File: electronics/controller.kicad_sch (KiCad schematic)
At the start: 88 parts, among them J1 Power_Supply_Connector, J10 Heated_Bed_Thermistor_Connect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, J11 Bl_Touch_Gnd_ZMin_Connector, J12 Bl_Touch_Signal_Vcc_Gnd_Conne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, J13 Motor_A_Connector, J14 Motor_B_Connector, J15 Motor_Z_Connector, J16 Motor_E_Connector, J2 X_Axis_Endstop_Connector, J3 Y_Axis_Endstop_Connector, J4 USB_C_Receptacle_USB2.0, J5 Hotend_Connector, J6 Heated_Bed_Connector, J7 Hotend_Fan_Connector, J8 Layer_Fan_Connector, J9 Hotend_Thermistor_Connector, Q1 PSMN4R1-30YLC, Q2 PSMN4R1-30YLC, Q3 PSMN4R1-30YLC, Q4 PSMN4R1-30YLC, SW1 EN_Button, SW2 Boot_Button, SW3 Pause/Resume_Button, U1 AZ1084CD-3.3TRG1, U10 MCU45P04-TP, U11 K7805MT-1000R4, U3 ESP32-S3-WROOM-1, U4 MT29F2G01ABAGDWB-IT, U5 USBLC6-2SC6, U6 TMC2209_SILENTSTEPSTICK, U7 TMC2209_SILENTSTEPSTICK, U8 TMC2209_SILENTSTEPSTICK, U9 TMC2209_SILENTSTEPSTICK

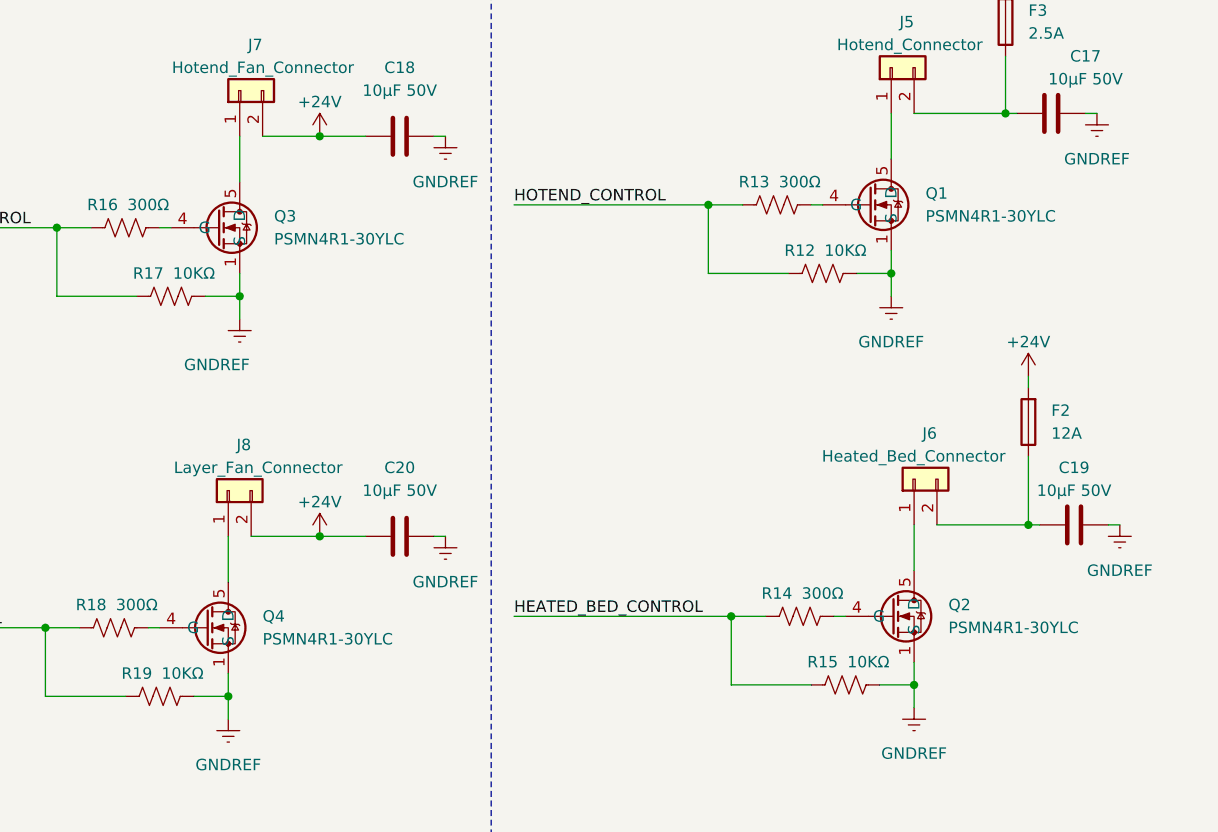
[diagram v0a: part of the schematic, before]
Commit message: ⚡️ Replace the PSMN4R1-30YLC mosfets with the appropriate ones on KiCad schematic
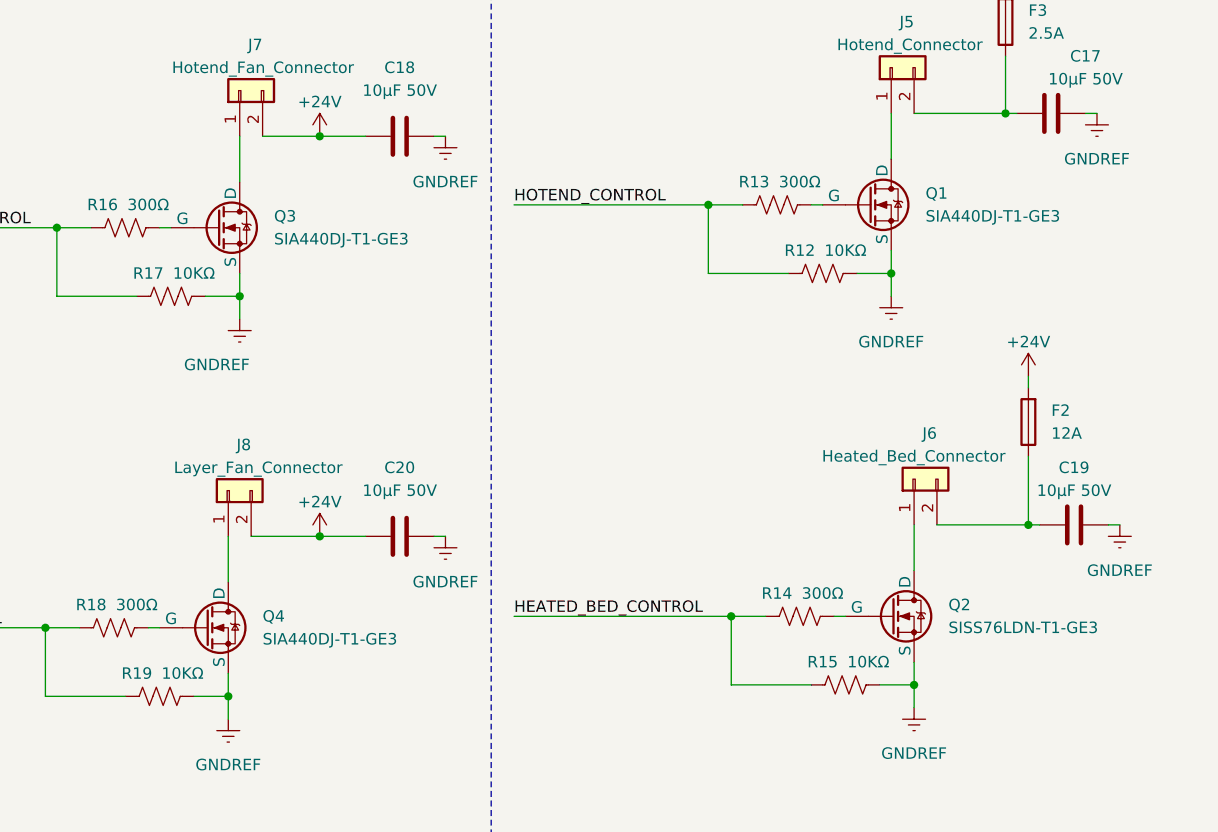
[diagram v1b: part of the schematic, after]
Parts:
- Q1, Q3, Q4: value PSMN4R1-30YLC -> SIA440DJ-T1-GE3; symbol Project:PSMN4R1-30YLC -> Project:NMOS
- Q2: value PSMN4R1-30YLC -> SISS76LDN-T1-GE3; symbol Project:PSMN4R1-30YLC -> Project:NMOS
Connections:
- net GNDREF: no longer Q1.1 (S), Q1.2 (S), Q2.1 (S), Q2.2 (S), Q3.1 (S), Q3.2 (S), Q4.1 (S), Q4.2 (S)
- net at J5.1 (Pin_1): now also Q1.1 (D); no longer Q1.5 (D)
- net at R14.2: now also Q2.2 (G); no longer Q2.4 (G)
- net at J6.1 (Pin_1): now also Q2.1 (D); no longer Q2.5 (D)
- net at R18.2: now also Q4.2 (G); no longer Q4.4 (G)
- net at J8.1 (Pin_1): now also Q4.1 (D); no longer Q4.5 (D)
- net at J7.1 (Pin_1): now also Q3.1 (D); no longer Q3.5 (D)
- net at R13.2: now also Q1.2 (G); no longer Q1.4 (G)
- net at R16.2: now also Q3.2 (G); no longer Q3.4 (G)
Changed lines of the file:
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@@
     )
   )
-  (symbol (lib_id "Project:PSMN4R1-30YLC") (at 374.65 228.6 0) (unit 1)
+  (symbol (lib_id "Project:NMOS") (at 374.65 228.6 0) (unit 1)
     (in_bom yes) (on_board yes) (dnp no) (fields_autoplaced)
     (property "Reference" "Q2" (at 381 227.33 0)
       (effects (font (size 1.27 1.27)) (justify left))
     )
-    (property "Value" "PSMN4R1-30YLC" (at 381 229.87 0)
+    (property "Value" "SISS76LDN-T1-GE3" (at 381 229.87 0)
       (effects (font (size 1.27 1.27)) (justify left))
     )
-    (property "Footprint" "Package_TO_SOT_SMD:LFPAK56" (at 378.46 228.6 0)
+    (property "Footprint" "Package_TO_SOT_SMD:LFPAK56" (at 379.73 226.06 0)
       (effects (font (size 1.27 1.27)) hide)
     )
-    (property "Datasheet" "https://assets.nexperia.com/documents/data-sheet/PSMN4R1-30YLC.pdf" (at 374.65 228.6 0)
+    (property "Datasheet" "https://ngspice.sourceforge.io/docs/ngspice-manual.pdf" (at 374.65 241.3 0)
+      (effects (font (size 1.27 1.27)) hide)
+    )
+    (property "Sim.Device" "NMOS" (at 374.65 245.745 0)
+      (effects (font (size 1.27 1.27)) hide)
+    )
+    (property "Sim.Type" "VDMOS" (at 374.65 247.65 0)
+      (effects (font (size 1.27 1.27)) hide)
+    )
+    (property "Sim.Pins" "1=D 2=G 3=S" (at 374.65 243.84 0)
       (effects (font (size 1.27 1.27)) hide)
     )
@@
     (pin "2")
     (pin "3")
-    (pin "4")
-    (pin "5")
     (instances
       (project "controller"
@@
     )
   )
-  (symbol (lib_id "Project:PSMN4R1-30YLC") (at 298.45 229.87 0) (unit 1)
+  (symbol (lib_id "Project:NMOS") (at 298.45 229.87 0) (unit 1)
     (in_bom yes) (on_board yes) (dnp no) (fields_autoplaced)
     (property "Reference" "Q4" (at 304.8 228.6 0)
       (effects (font (size 1.27 1.27)) (justify left))
     )
-    (property "Value" "PSMN4R1-30YLC" (at 304.8 231.14 0)
+    (property "Value" "SIA440DJ-T1-GE3" (at 304.8 231.14 0)
       (effects (font (size 1.27 1.27)) (justify left))
     )
-    (property "Footprint" "Package_TO_SOT_SMD:LFPAK56" (at 302.26 229.87 0)
+    (property "Footprint" "Package_TO_SOT_SMD:LFPAK56" (at 303.53 227.33 0)
       (effects (font (size 1.27 1.27)) hide)
     )
-    (property "Datasheet" "https://assets.nexperia.com/documents/data-sheet/PSMN4R1-30YLC.pdf" (at 298.45 229.87 0)
+    (property "Datasheet" "https://ngspice.sourceforge.io/docs/ngspice-manual.pdf" (at 298.45 242.57 0)
+      (effects (font (size 1.27 1.27)) hide)
+    )
+    (property "Sim.Device" "NMOS" (at 298.45 247.015 0)
+      (effects (font (size 1.27 1.27)) hide)
+    )
+    (property "Sim.Type" "VDMOS" (at 298.45 248.92 0)
+      (effects (font (size 1.27 1.27)) hide)
+    )
+    (property "Sim.Pins" "1=D 2=G 3=S" (at 298.45 245.11 0)
       (effects (font (size 1.27 1.27)) hide)
     )
@@
     (pin "2")
     (pin "3")
-    (pin "4")
-    (pin "5")
     (instances
       (project "controller"
@@
     )
   )
-  (symbol (lib_id "Project:PSMN4R1-30YLC") (at 372.11 182.88 0) (unit 1)
+  (symbol (lib_id "Project:NMOS") (at 372.11 182.88 0) (unit 1)
     (in_bom yes) (on_board yes) (dnp no) (fields_autoplaced)
     (property "Reference" "Q1" (at 378.46 181.61 0)
       (effects (font (size 1.27 1.27)) (justify left))
     )
-    (property "Value" "PSMN4R1-30YLC" (at 378.46 184.15 0)
+    (property "Value" "SIA440DJ-T1-GE3" (at 378.46 184.15 0)
       (effects (font (size 1.27 1.27)) (justify left))
     )
-    (property "Footprint" "Package_TO_SOT_SMD:LFPAK56" (at 375.92 182.88 0)
+    (property "Footprint" "Package_TO_SOT_SMD:LFPAK56" (at 377.19 180.34 0)
       (effects (font (size 1.27 1.27)) hide)
     )
-    (property "Datasheet" "https://assets.nexperia.com/documents/data-sheet/PSMN4R1-30YLC.pdf" (at 372.11 182.88 0)
+    (property "Datasheet" "https://ngspice.sourceforge.io/docs/ngspice-manual.pdf" (at 372.11 195.58 0)
+      (effects (font (size 1.27 1.27)) hide)
+    )
+    (property "Sim.Device" "NMOS" (at 372.11 200.025 0)
+      (effects (font (size 1.27 1.27)) hide)
+    )
+    (property "Sim.Type" "VDMOS" (at 372.11 201.93 0)
+      (effects (font (size 1.27 1.27)) hide)
+    )
+    (property "Sim.Pins" "1=D 2=G 3=S" (at 372.11 198.12 0)
       (effects (font (size 1.27 1.27)) hide)
     )
@@
     (pin "2")
     (pin "3")
-    (pin "4")
-    (pin "5")
     (instances
       (project "controller"
@@
     )
   )
-  (symbol (lib_id "Project:PSMN4R1-30YLC") (at 299.72 185.42 0) (unit 1)
+  (symbol (lib_id "Project:NMOS") (at 299.72 185.42 0) (unit 1)
     (in_bom yes) (on_board yes) (dnp no) (fields_autoplaced)
     (property "Reference" "Q3" (at 306.07 184.15 0)
       (effects (font (size 1.27 1.27)) (justify left))
     )
-    (property "Value" "PSMN4R1-30YLC" (at 306.07 186.69 0)
+    (property "Value" "SIA440DJ-T1-GE3" (at 306.07 186.69 0)
       (effects (font (size 1.27 1.27)) (justify left))
     )
-    (property "Footprint" "Package_TO_SOT_SMD:LFPAK56" (at 303.53 185.42 0)
+    (property "Footprint" "Package_TO_SOT_SMD:LFPAK56" (at 304.8 182.88 0)
       (effects (font (size 1.27 1.27)) hide)
     )
-    (property "Datasheet" "https://assets.nexperia.com/documents/data-sheet/PSMN4R1-30YLC.pdf" (at 299.72 185.42 0)
+    (property "Datasheet" "https://ngspice.sourceforge.io/docs/ngspice-manual.pdf" (at 299.72 198.12 0)
+      (effects (font (size 1.27 1.27)) hide)
+    )
+    (property "Sim.Device" "NMOS" (at 299.72 202.565 0)
+      (effects (font (size 1.27 1.27)) hide)
+    )
+    (property "Sim.Type" "VDMOS" (at 299.72 204.47 0)
+      (effects (font (size 1.27 1.27)) hide)
+    )
+    (property "Sim.Pins" "1=D 2=G 3=S" (at 299.72 200.66 0)
       (effects (font (size 1.27 1.27)) hide)
     )
@@
     (pin "2")
     (pin "3")
-    (pin "4")
-    (pin "5")
     (instances
       (project "controller"

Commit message: ⚰️ Remove unused symbols on KiCad
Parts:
- U10: symbol Project:MCU45P04-TP -> Project:PMOS
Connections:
- net at D1.1 (K), F1.1, U10.3 (S): no longer U10.1 (S), U10.2 (S)
- net at D1.2 (A), R26.1: now also U10.2 (G); no longer U10.4 (G)
- net at J1.2 (Pin_2): now also U10.1 (D); no longer U10.5 (D)
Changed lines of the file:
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@@
     )
   )
-  (symbol (lib_id "Project:MCU45P04-TP") (at 33.02 48.26 0) (mirror y) (unit 1)
+  (symbol (lib_id "Project:PMOS") (at 34.29 48.26 0) (mirror y) (unit 1)
     (in_bom yes) (on_board yes) (dnp no)
-    (property "Reference" "U10" (at 27.94 49.53 0)
+    (property "Reference" "U10" (at 29.21 49.53 0)
       (effects (font (size 1.27 1.27)) (justify left))
     )
-    (property "Value" "MCU45P04-TP" (at 27.94 46.99 0)
+    (property "Value" "MCU45P04-TP" (at 29.21 46.99 0)
       (effects (font (size 1.27 1.27)) (justify left))
     )
-    (property "Footprint" "" (at 33.02 48.26 0)
+    (property "Footprint" "" (at 29.21 45.72 0)
       (effects (font (size 1.27 1.27)) hide)
     )
-    (property "Datasheet" "https://www.mccsemi.com/pdf/Products/MCU45P04(DPAK).pdf" (at 33.02 62.23 0)
+    (property "Datasheet" "https://ngspice.sourceforge.io/docs/ngspice-manual.pdf" (at 34.29 60.96 0)
+      (effects (font (size 1.27 1.27)) hide)
+    )
+    (property "Sim.Device" "PMOS" (at 34.29 65.405 0)
+      (effects (font (size 1.27 1.27)) hide)
+    )
+    (property "Sim.Type" "VDMOS" (at 34.29 67.31 0)
+      (effects (font (size 1.27 1.27)) hide)
+    )
+    (property "Sim.Pins" "1=D 2=G 3=S" (at 34.29 63.5 0)
       (effects (font (size 1.27 1.27)) hide)
     )
@@
     (pin "2")
     (pin "3")
-    (pin "4")
-    (pin "5")
     (instances
       (project "controller"

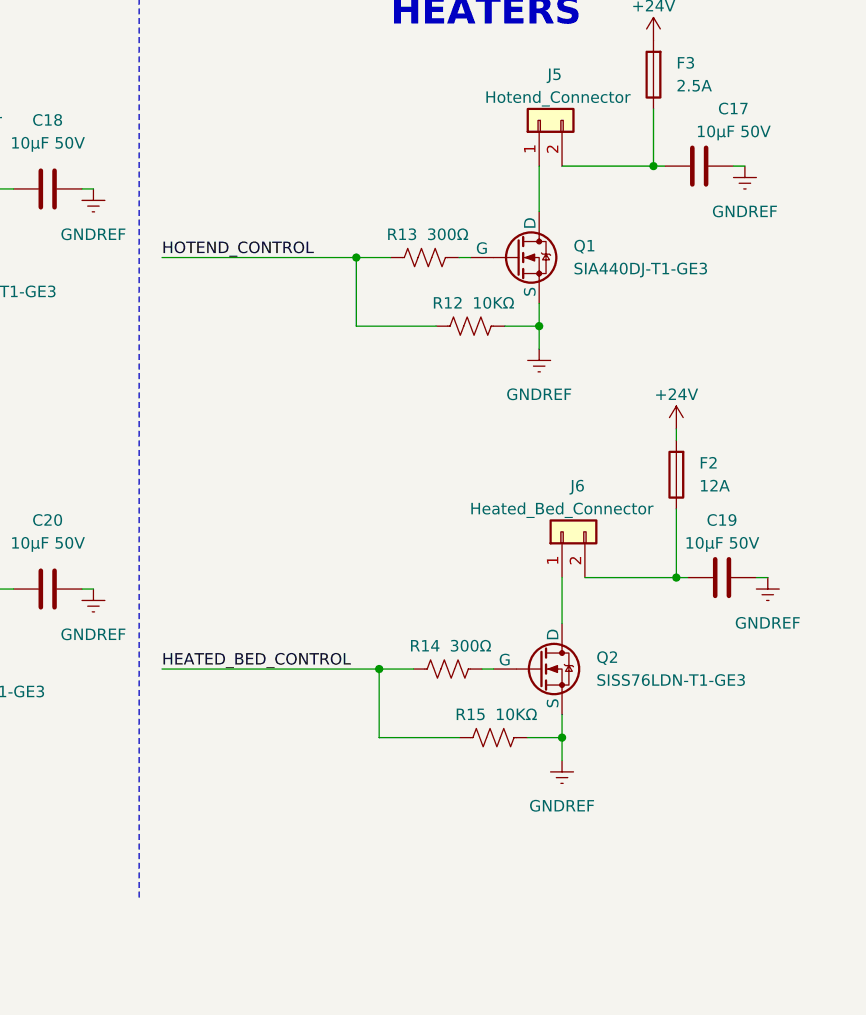
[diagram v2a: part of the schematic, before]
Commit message: ✨ Add flyback diodes to heaters on KiCad schematic
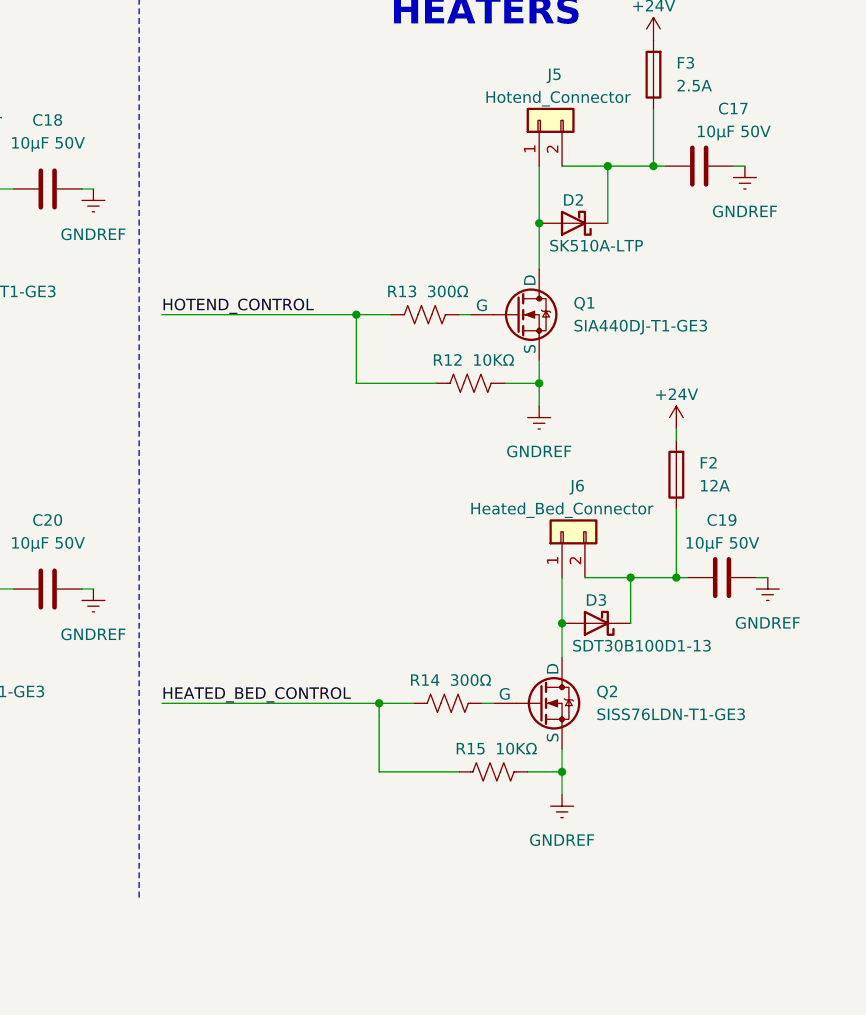
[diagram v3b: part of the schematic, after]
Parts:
- added D2: SK510A-LTP, symbol Project:D_Schottky
- added D3: SDT30B100D1-13, symbol Project:D_Schottky
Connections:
- net at J5.1 (Pin_1), Q1.1 (D): now also D2.2 (A)
- net at C17.1, F3.1, J5.2 (Pin_2): now also D2.1 (K)
- net at C19.1, F2.1, J6.2 (Pin_2): now also D3.1 (K)
- net at J6.1 (Pin_1), Q2.1 (D): now also D3.2 (A)
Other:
- moved on the sheet: Q1, Q2, R12, R13, R14, R15
